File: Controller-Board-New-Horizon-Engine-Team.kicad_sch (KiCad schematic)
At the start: 0 parts

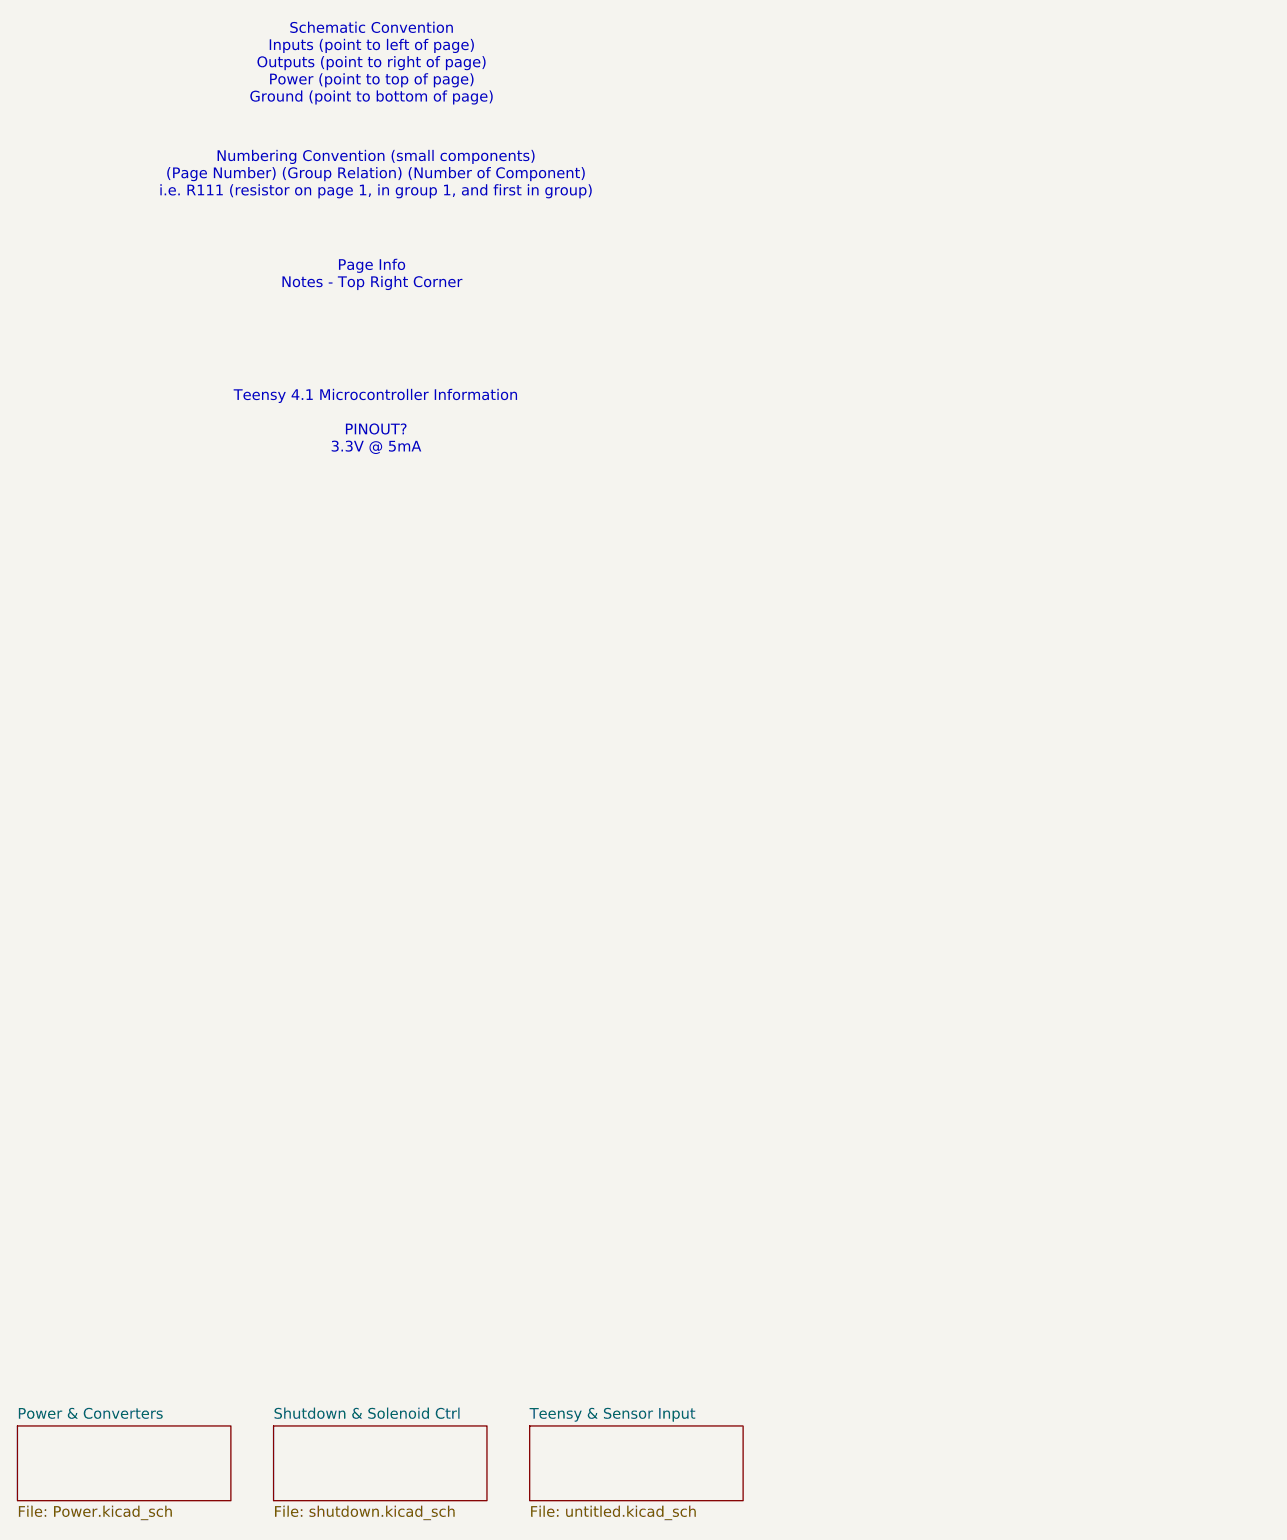
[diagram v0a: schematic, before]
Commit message: Teensy Pins, SDC, Fault Signal Construction
*4 Additional Signal Input Filters
*SDC Completed (need component selection)
*Test points added
*Fault Signal Construction using comparators (more quick, more accurate than voltage divider)
*Considerations: noise - construction of pcb, additional filters; faults - latching, teensy (complete control), fault signals - testing required
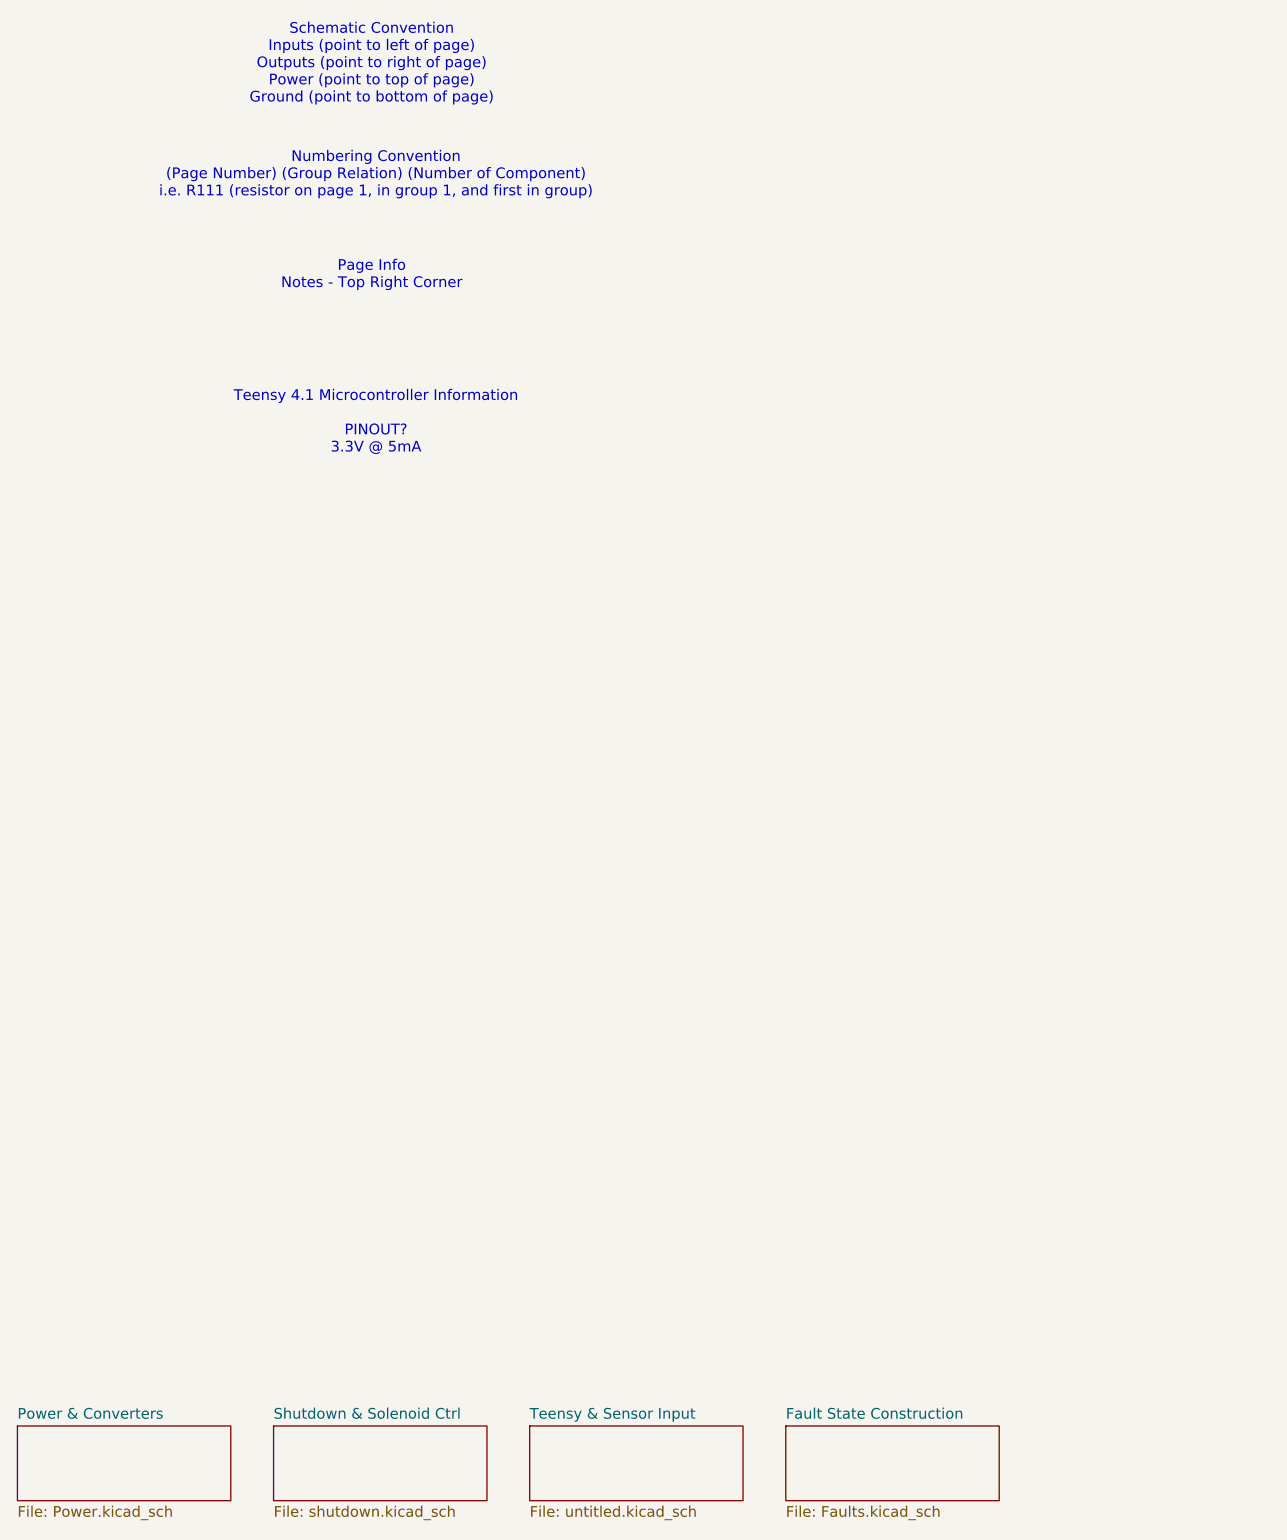
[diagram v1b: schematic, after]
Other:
- added sheet Fault State Construction (Faults.kicad_sch)
- note added: "Numbering Convention (Page Number) (Group Relation) (Number of Component) i.e. R111 (resistor on page 1, in group 1, and first in group)"
- note removed: "Numbering Convention (small components) (Page Number) (Group Relation) (Number of Component) i.e. R111 (resistor on page 1, in group 1, and first in group)"
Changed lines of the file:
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@@
 		(company "New Horizon Engine Team")
 	)
-	(text "Numbering Convention (small components)\n(Page Number) (Group Relation) (Number of Component)\ni.e. R111 (resistor on page 1, in group 1, and first in group)"
+	(text "Numbering Convention\n(Page Number) (Group Relation) (Number of Component)\ni.e. R111 (resistor on page 1, in group 1, and first in group)"
 		(exclude_from_sim no)
 		(at 60.452 34.036 0)
@@
 		)
 		(instances
-			(project "rocket"
+			(project "Controller-Board-New-Horizon-Engine-Team"
 				(path "/5af55672-b395-4e4d-9412-3e1b639bac31"
 					(page "3")
@@
 		)
 		(instances
-			(project "rocket"
+			(project "Controller-Board-New-Horizon-Engine-Team"
 				(path "/5af55672-b395-4e4d-9412-3e1b639bac31"
 					(page "2")
@@
 	)
 	(sheet
+		(at 109.22 182.88)
+		(size 25.4 8.89)
+		(exclude_from_sim no)
+		(in_bom yes)
+		(on_board yes)
+		(dnp no)
+		(fields_autoplaced yes)
+		(stroke
+			(width 0.1524)
+			(type solid)
+		)
+		(fill
+			(color 0 0 0 0.0000)
+		)
+		(property "Sheetname" "Fault State Construction"
+			(at 109.22 182.1684 0)
+			(effects
+				(font
+					(size 1.27 1.27)
+				)
+				(justify left bottom)
+			)
+		)
+		(property "Sheetfile" "Faults.kicad_sch"
+			(at 109.22 192.3546 0)
+			(effects
+				(font
+					(size 1.27 1.27)
+				)
+				(justify left top)
+			)
+		)
+		(instances
+			(project "Controller-Board-New-Horizon-Engine-Team"
+				(path "/5af55672-b395-4e4d-9412-3e1b639bac31"
+					(page "5")
+				)
+			)
+		)
+	)
+	(sheet
 		(at 78.74 182.88)
 		(size 25.4 8.89)
@@
 		)
 		(instances
-			(project "rocket"
+			(project "Controller-Board-New-Horizon-Engine-Team"
 				(path "/5af55672-b395-4e4d-9412-3e1b639bac31"
 					(page "4")

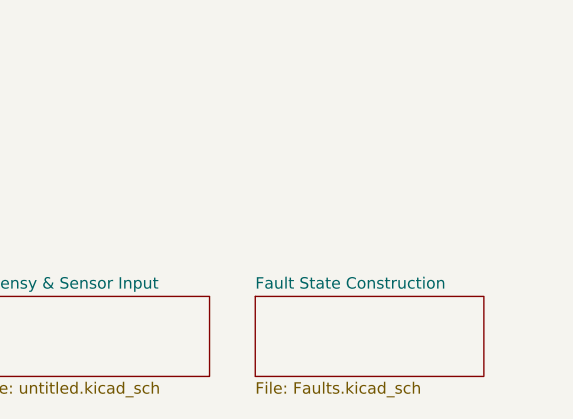
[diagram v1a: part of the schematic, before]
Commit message: Purge Oscillator/Timer
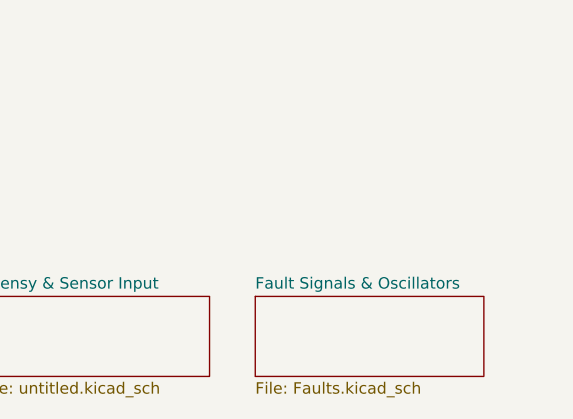
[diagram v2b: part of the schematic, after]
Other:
- sheet Fault State Construction renamed Fault Signals & Oscillators
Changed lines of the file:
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@@
 			(color 0 0 0 0.0000)
 		)
-		(property "Sheetname" "Fault State Construction"
+		(property "Sheetname" "Fault Signals & Oscillators"
 			(at 109.22 182.1684 0)
 			(effects

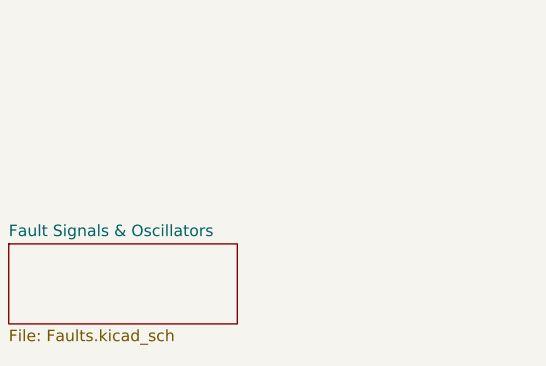
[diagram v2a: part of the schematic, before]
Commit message: Voltage Fix, Tri-State Buffers, Double-Buffer
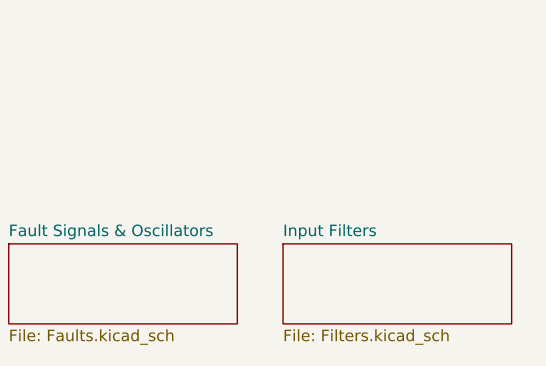
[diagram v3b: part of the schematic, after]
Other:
- added sheet Input Filters (Filters.kicad_sch)
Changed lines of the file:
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@@
+	)
+	(sheet
+		(at 139.7 182.88)
+		(size 25.4 8.89)
+		(exclude_from_sim no)
+		(in_bom yes)
+		(on_board yes)
+		(dnp no)
+		(fields_autoplaced yes)
+		(stroke
+			(width 0.1524)
+			(type solid)
+		)
+		(fill
+			(color 0 0 0 0.0000)
+		)
+		(property "Sheetname" "Input Filters"
+			(at 139.7 182.1684 0)
+			(effects
+				(font
+					(size 1.27 1.27)
+				)
+				(justify left bottom)
+			)
+		)
+		(property "Sheetfile" "Filters.kicad_sch"
+			(at 139.7 192.3546 0)
+			(effects
+				(font
+					(size 1.27 1.27)
+				)
+				(justify left top)
+			)
+		)
+		(instances
+			(project "Controller-Board-New-Horizon-Engine-Team"
+				(path "/5af55672-b395-4e4d-9412-3e1b639bac31"
+					(page "6")
+				)
+			)
+		)
 	)
 	(sheet
